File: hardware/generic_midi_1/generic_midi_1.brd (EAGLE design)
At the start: 47.3 x 44.8 mm, 20 parts, among them IC1 MEGA168/328, IC2 RFM12

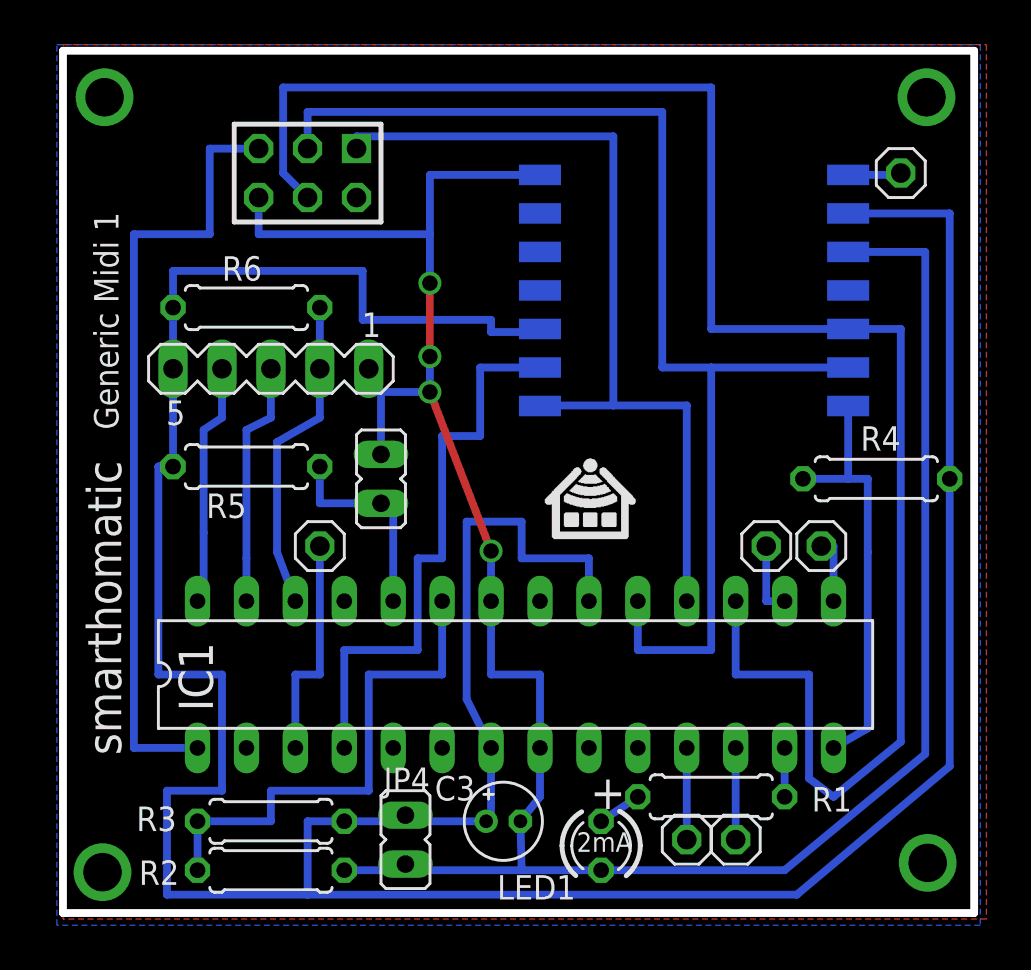
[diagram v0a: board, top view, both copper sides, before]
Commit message: add/rename some files, add I2C resistors to midi PCB
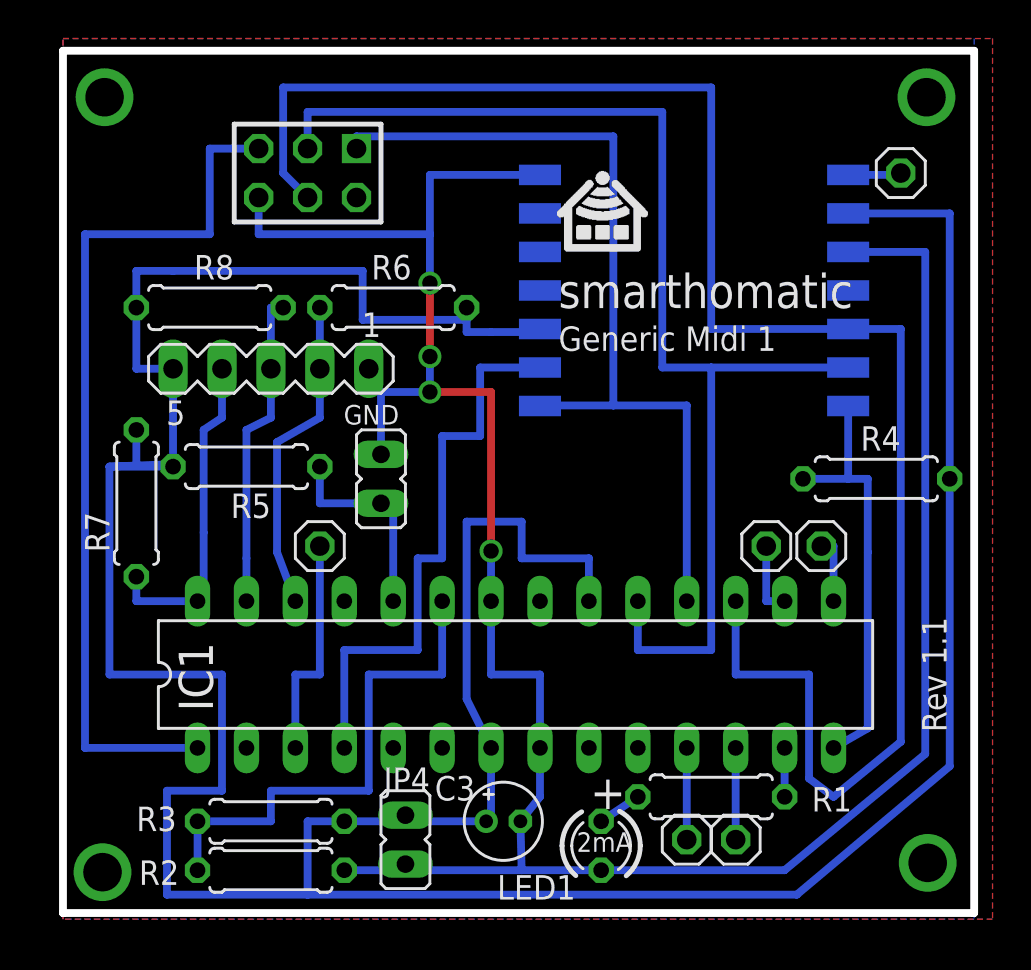
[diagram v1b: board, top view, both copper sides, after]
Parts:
- added R7, R8: 10k, rcl:0207/7
- JP2: value SHT15 -> I/O
- moved R6 7.62 mm to (17.1, 31.8), turned to 180 degrees
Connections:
- net N$7: now also R8.1
- net N$9: now also R7.1
- net VCC: now also R7.2, R8.2
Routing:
- net VCC: track 179.4 -> 193.9 mm
- net N$8: track 40.9 -> 46.0 mm
- net N$9: track 12.8 -> 17.3 mm
- net N$7: track 12.8 -> 16.7 mm
- net GND: track 126.1 -> 128.7 mm
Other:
- board text added: "GND"
- board text added: "Rev 1.1"
- board text removed: "Rev 1.0"

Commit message: update generic midi PCB
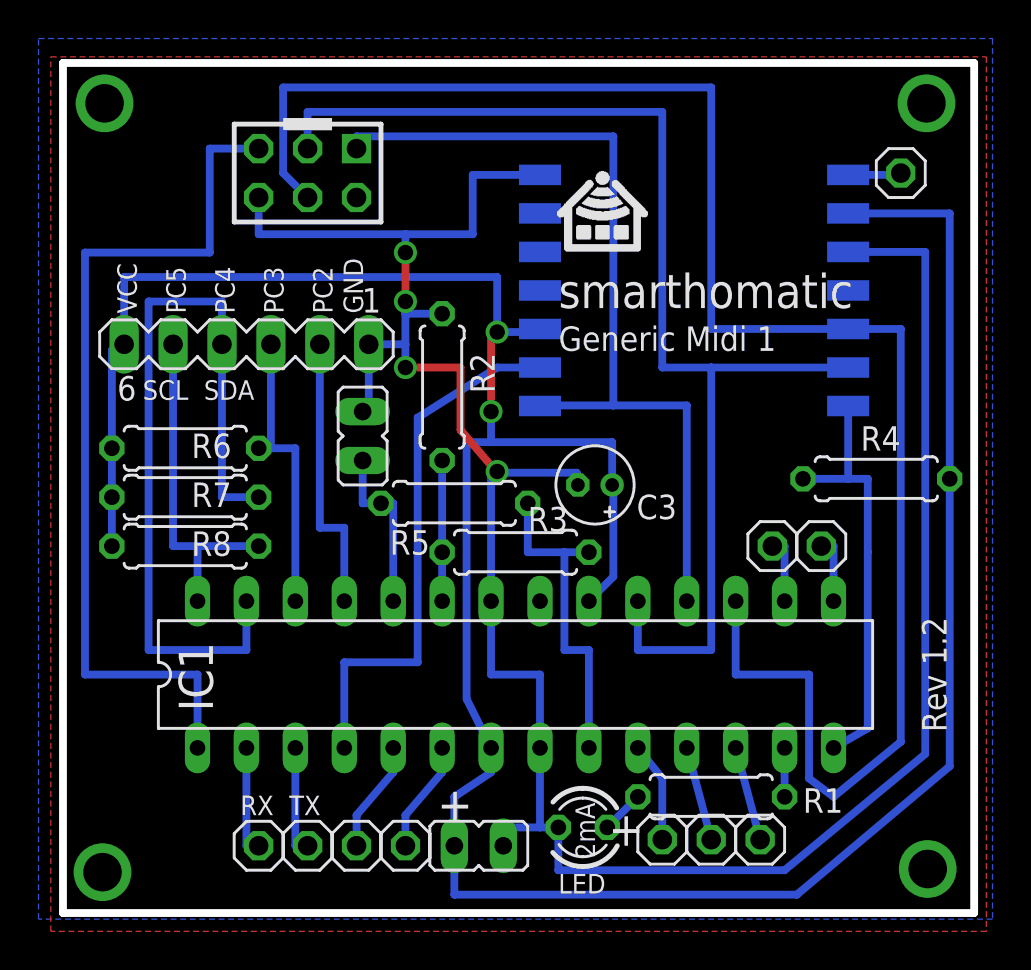
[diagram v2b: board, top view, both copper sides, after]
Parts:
- removed LED1: 2mA, led:LED3MM
- added JP11: PD4, pinhead:1X01
- added JP12: PD3, pinhead:1X01
- added JP13: PB7, pinhead:1X01
- added JP14: PD0, pinhead:1X01
- added LED: 2mA, led:LED3MM
- JP2: device con-lstb:MA05-1 -> con-lstb:MA06-1
- JP8: value PD1/TX -> PD1
- moved R2 26.6 mm to (19.7, 27.6), turned to 270 degrees
- moved R3 18.9 mm to (23.5, 19.1)
- moved C3 18.1 mm to (27.6, 22.5), turned to 180 degrees
- moved JP8 15.6 mm to (12.7, 3.81)
- moved R6 13.0 mm to (6.35, 24.4), turned to 0 degrees
- moved R8 12.4 mm to (6.35, 19.4)
- moved R5 11.0 mm to (20.3, 21.6), turned to 0 degrees
- moved JP4 3.82 mm to (21.6, 3.81), turned to 90 degrees
- moved R7 2.56 mm to (6.35, 21.9), turned to 180 degrees
- moved JP3 2.42 mm to (15.6, 25.1)
- moved JP2 1.80 mm to (9.53, 29.8)
- moved JP10 1.27 mm to (36.2, 4.13)
- moved JP9 1.27 mm to (33.7, 4.13)
- moved JP7 0.32 mm to (36.8, 19.4)
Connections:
- new net N$21: IC1.25, JP2.2
- new net N$22: IC1.6, JP11.1
- new net N$23: IC1.5, JP12.1
- new net N$24: IC1.9, R3.2, R5.2
- new net N$25: IC1.10, JP13.1
- new net N$26: IC1.2, JP14.1
- net GND: now also LED.K; no longer LED1.K
- net N$10: now also JP2.3; no longer JP2.2
- net N$12: now also LED.A; no longer LED1.A
- net N$7: now also JP2.4, R7.1; no longer JP2.3, R8.1
- net N$9: now also JP2.5, R8.1; no longer JP2.4, R7.1
- net VCC: now also JP2.6; no longer JP2.5, R3.2, R5.2
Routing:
- net VCC: track 193.9 -> 148.3 mm, vias 0 -> 2
- net N$7: track 16.7 -> 41.6 mm
- net N$18: track 26.7 -> 7.30 mm
- net N$24: track 0.00 -> 17.1 mm
- net N$21: track 0.00 -> 14.6 mm
- net N$20: track 11.7 -> 5.71 mm
- net N$23: track 0.00 -> 5.78 mm
- net N$22: track 0.00 -> 5.78 mm
- net N$26: track 0.00 -> 5.71 mm
- net N$25: track 0.00 -> 5.21 mm
- net N$1: track 10.8 -> 8.89 mm
- net N$15: track 29.9 -> 28.1 mm
- net GND: track 128.7 -> 127.0 mm
- net N$10: track 16.7 -> 15.9 mm
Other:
- board size 47.3 x 44.8 mm -> 47.3 x 44.1 mm
- board text added: "PC2"
- board text added: "PC3"
- board text added: "PC4"
- board text added: "PC5"
- board text added: "RX"
- board text added: "Rev 1.2"
- board text added: "SCL"
- board text added: "SDA"
- board text added: "TX"
- board text added: "VCC"
- board text removed: "Rev 1.1"

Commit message: Add pull-up resistor for possible one-wire sensor on PD4.
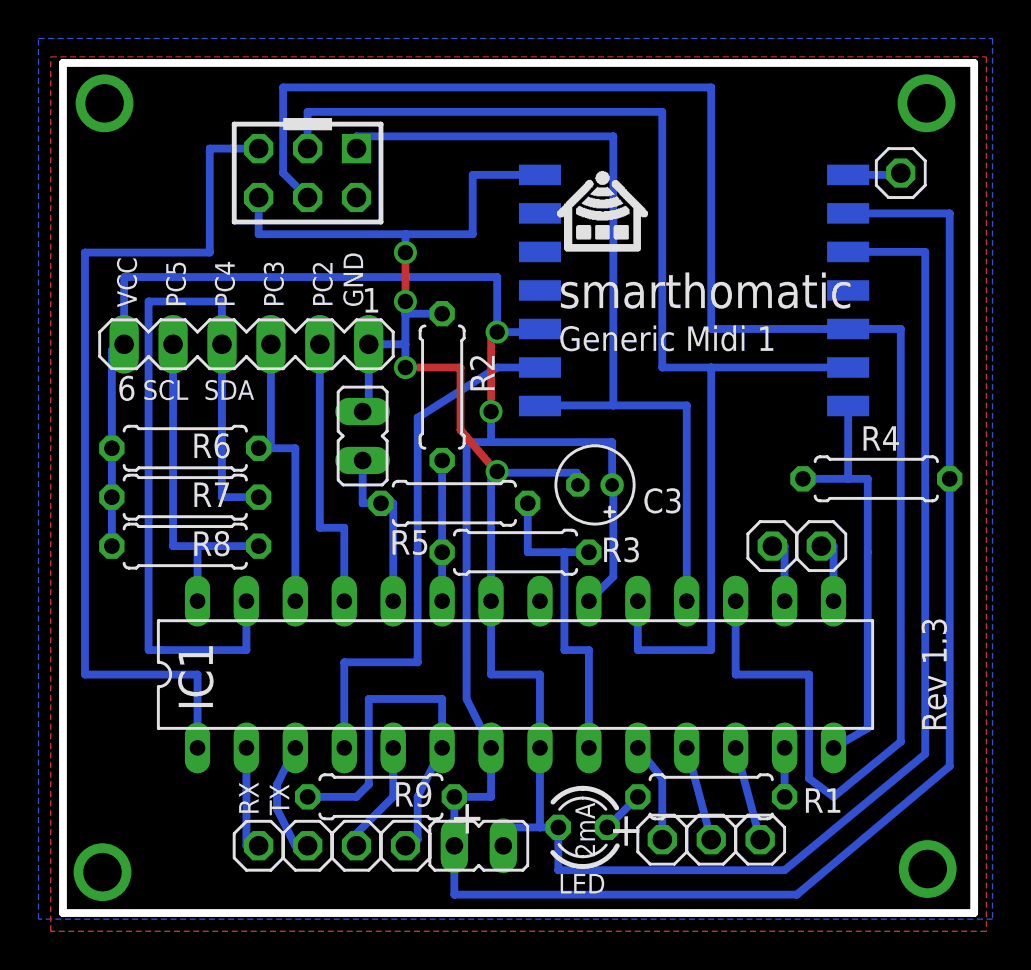
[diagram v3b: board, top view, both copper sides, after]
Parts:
- added R9: 4k7, rcl:0207/7
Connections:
- net N$22: now also R9.1
- net VCC: now also R9.2
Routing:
- net N$22: track 5.78 -> 20.0 mm
- net VCC: track 148.3 -> 149.2 mm
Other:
- board text added: "Rev 1.3"
- board text removed: "Rev 1.2"
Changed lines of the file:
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@@
 <wire x1="47.3075" y1="0.3175" x2="0" y2="0.3175" width="0.4064" layer="20"/>
 <text x="25.7302" y="31.7246" size="1.778" layer="25" font="vector">smarthomatic</text>
-<text x="44.6024" y="15.6845" size="1.27" layer="25" rot="R270">Rev 1.2</text>
+<text x="44.6024" y="15.6845" size="1.27" layer="25" rot="R270">Rev 1.3</text>
 <rectangle x1="26.109928125" y1="34.65195" x2="29.907228125" y2="34.68496875" layer="25"/>
 <rectangle x1="26.076909375" y1="34.68496875" x2="29.973265625" y2="34.7179875" layer="25"/>
@@
 <text x="30.1625" y="3.81" size="1.778" layer="25" rot="MR0">+</text>
 <text x="27.6225" y="3.175" size="1.016" layer="25" rot="R90">2mA</text>
-<text x="15.5829" y="31.4452" size="1.016" layer="25" rot="R90">GND</text>
-<text x="21.2725" y="5.08" size="1.778" layer="25" rot="MR0">+</text>
+<text x="15.5829" y="31.7627" size="1.016" layer="25" rot="R90">GND</text>
+<text x="21.9075" y="4.445" size="1.778" layer="25" rot="MR0">+</text>
 <rectangle x1="11.43" y1="40.9575" x2="13.97" y2="41.5925" layer="21"/>
-<text x="9.2075" y="5.3975" size="1.016" layer="25">RX</text>
-<text x="11.7475" y="5.3975" size="1.016" layer="25">TX</text>
-<text x="3.8354" y="31.4452" size="1.016" layer="25" rot="R90">VCC</text>
-<text x="13.9954" y="31.4452" size="1.016" layer="25" rot="R90">PC2</text>
-<text x="11.4554" y="31.4452" size="1.016" layer="25" rot="R90">PC3</text>
-<text x="8.9154" y="31.4452" size="1.016" layer="25" rot="R90">PC4</text>
-<text x="6.3754" y="31.4452" size="1.016" layer="25" rot="R90">PC5</text>
+<text x="10.16" y="5.3975" size="1.016" layer="25" rot="R90">RX</text>
+<text x="11.7475" y="5.3975" size="1.016" layer="25" rot="R90">TX</text>
+<text x="3.8354" y="31.7627" size="1.016" layer="25" rot="R90">VCC</text>
+<text x="13.9954" y="31.7627" size="1.016" layer="25" rot="R90">PC2</text>
+<text x="11.4554" y="31.7627" size="1.016" layer="25" rot="R90">PC3</text>
+<text x="8.9154" y="31.7627" size="1.016" layer="25" rot="R90">PC4</text>
+<text x="6.3754" y="31.7627" size="1.016" layer="25" rot="R90">PC5</text>
 <text x="7.3152" y="26.9621" size="1.016" layer="25">SDA</text>
 <text x="4.1402" y="26.9621" size="1.016" layer="25">SCL</text>
@@
 </element>
 <element name="C3" library="rcl" package="E1,8-4" value="10µ" x="27.6225" y="22.5425" smashed="yes" rot="R180">
-<attribute name="NAME" x="29.7815" y="20.7645" size="1.27" layer="25" ratio="10"/>
-<attribute name="VALUE" x="29.7815" y="22.352" size="1.27" layer="27" ratio="10"/>
+<attribute name="NAME" x="30.099" y="21.082" size="1.27" layer="25" ratio="10"/>
+<attribute name="VALUE" x="30.099" y="22.6695" size="1.27" layer="27" ratio="10"/>
 </element>
 <element name="R2" library="rcl" package="0207/7" value="150k" x="19.685" y="27.6225" smashed="yes" rot="R270">
@@
 </element>
 <element name="R3" library="rcl" package="0207/7" value="330k" x="23.495" y="19.05" smashed="yes">
-<attribute name="NAME" x="24.13" y="20.1295" size="1.27" layer="25" ratio="10"/>
+<attribute name="NAME" x="27.94" y="18.542" size="1.27" layer="25" ratio="10"/>
 <attribute name="VALUE" x="25.4635" y="19.6088" size="1.27" layer="27" ratio="10" rot="R180"/>
 </element>
@@
 </element>
 <element name="JP3" library="jumper" package="JP1" value="PHOTO" x="15.5575" y="25.0825" smashed="yes" rot="R180">
-<attribute name="VALUE" x="14.0335" y="23.1775" size="0.8128" layer="27" ratio="10" rot="R90"/>
+<attribute name="VALUE" x="13.716" y="23.1775" size="0.8128" layer="27" ratio="10" rot="R90"/>
 </element>
 <element name="JP4" library="jumper" package="JP1" value="PWR" x="21.59" y="3.81" smashed="yes" rot="R90">
@@
 <element name="JP14" library="pinhead" package="1X01" value="PD0" x="10.16" y="3.81" smashed="yes">
 <attribute name="VALUE" x="7.9375" y="1.27" size="1.016" layer="27"/>
+</element>
+<element name="R9" library="rcl" package="0207/7" value="4k7" x="16.51" y="6.35" smashed="yes">
+<attribute name="NAME" x="17.145" y="5.842" size="1.27" layer="25" ratio="10"/>
+<attribute name="VALUE" x="13.589" y="5.7912" size="1.27" layer="27" ratio="10"/>
 </element>
 </elements>
@@
 <wire x1="2.54" y1="21.9075" x2="2.54" y2="19.3675" width="0.4064" layer="16"/>
 <wire x1="20.32" y1="3.81" x2="20.32" y2="1.27" width="0.4064" layer="16"/>
-<wire x1="20.32" y1="3.81" x2="20.32" y2="6.35" width="0.4064" layer="16"/>
-<wire x1="20.32" y1="6.35" x2="22.225" y2="7.62" width="0.4064" layer="16"/>
 <wire x1="22.225" y1="7.62" x2="22.225" y2="8.89" width="0.4064" layer="16"/>
+<contactref element="R9" pad="2"/>
+<wire x1="20.32" y1="6.35" x2="22.225" y2="6.35" width="0.4064" layer="16"/>
+<wire x1="22.225" y1="6.35" x2="22.225" y2="7.62" width="0.4064" layer="16"/>
 <wire x1="28.5115" y1="22.5425" x2="28.575" y2="22.5425" width="0" layer="19" extent="16-16"/>
+<wire x1="20.32" y1="6.35" x2="20.32" y2="3.81" width="0.4064" layer="16"/>
 </signal>
 <signal name="N$3">
@@
 <contactref element="JP8" pad="1"/>
 <wire x1="12.7" y1="3.81" x2="12.065" y2="3.81" width="0.4064" layer="16"/>
-<wire x1="12.065" y1="3.81" x2="12.065" y2="8.89" width="0.4064" layer="16"/>
+<wire x1="12.065" y1="3.81" x2="11.1125" y2="5.715" width="0.4064" layer="16"/>
+<wire x1="11.1125" y1="5.715" x2="11.1125" y2="6.985" width="0.4064" layer="16"/>
+<wire x1="11.1125" y1="6.985" x2="12.065" y2="8.89" width="0.4064" layer="16"/>
 </signal>
 <signal name="N$21">
@@
 <contactref element="IC1" pad="6"/>
 <contactref element="JP11" pad="1"/>
-<wire x1="17.78" y1="3.81" x2="17.78" y2="5.3975" width="0.4064" layer="16"/>
-<wire x1="17.78" y1="5.3975" x2="19.685" y2="7.62" width="0.4064" layer="16"/>
-<wire x1="19.685" y1="7.62" x2="19.685" y2="8.89" width="0.4064" layer="16"/>
+<wire x1="17.78" y1="3.81" x2="18.415" y2="4.1275" width="0.4064" layer="16"/>
+<wire x1="18.415" y1="4.1275" x2="18.415" y2="6.35" width="0.4064" layer="16"/>
+<wire x1="18.415" y1="6.35" x2="19.685" y2="8.89" width="0.4064" layer="16"/>
+<contactref element="R9" pad="1"/>
+<wire x1="12.7" y1="6.35" x2="15.24" y2="6.35" width="0.4064" layer="16"/>
+<wire x1="15.24" y1="6.35" x2="15.875" y2="6.985" width="0.4064" layer="16"/>
+<wire x1="15.875" y1="6.985" x2="15.875" y2="11.43" width="0.4064" layer="16"/>
+<wire x1="15.875" y1="11.43" x2="19.685" y2="11.43" width="0.4064" layer="16"/>
+<wire x1="19.685" y1="11.43" x2="19.685" y2="8.89" width="0.4064" layer="16"/>
 </signal>
 <signal name="N$23">
 <contactref element="IC1" pad="5"/>
 <contactref element="JP12" pad="1"/>
-<wire x1="15.24" y1="3.81" x2="15.24" y2="5.3975" width="0.4064" layer="16"/>
-<wire x1="15.24" y1="5.3975" x2="17.145" y2="7.62" width="0.4064" layer="16"/>
-<wire x1="17.145" y1="7.62" x2="17.145" y2="8.89" width="0.4064" layer="16"/>
+<wire x1="15.24" y1="3.81" x2="15.24" y2="4.445" width="0.4064" layer="16"/>
+<wire x1="15.24" y1="4.445" x2="17.145" y2="6.35" width="0.4064" layer="16"/>
+<wire x1="17.145" y1="6.35" x2="17.145" y2="8.89" width="0.4064" layer="16"/>
 </signal>
 <signal name="N$24">

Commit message: Add solder jumper to PCB for ISP VCC pin.
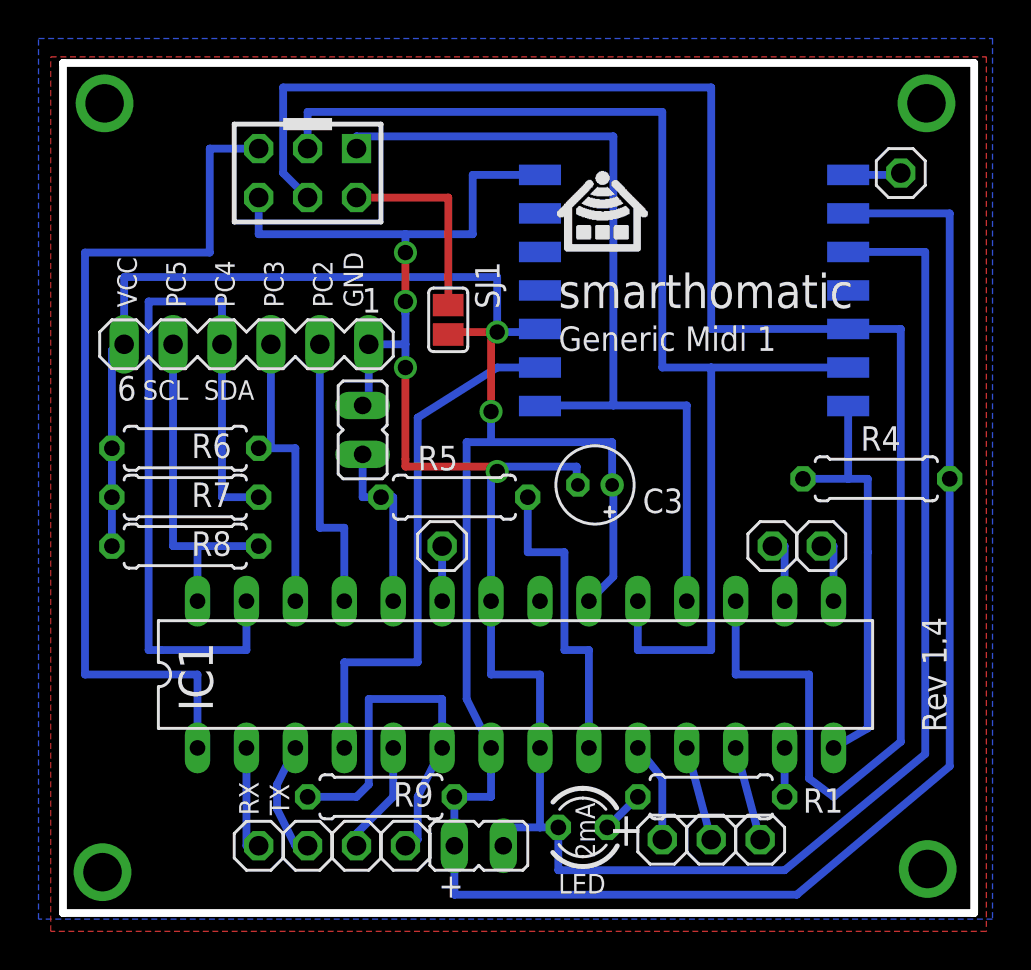
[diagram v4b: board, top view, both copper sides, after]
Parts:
- removed R2: 150k, rcl:0207/7
- removed R3: 330k, rcl:0207/7
- added JP15: PC0, pinhead:1X01
- added SJ1: VCC, jumper:SJ
- moved JP3 0.32 mm to (15.6, 25.4)
- moved R5 0.32 mm to (20.3, 21.9)
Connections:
- new net N$27: JP1.2, SJ1.1
- net GND: no longer R2.1
- net N$18: now also JP15.1; no longer R2.2, R3.1
- net N$24: no longer R3.2
- net VCC: now also SJ1.2
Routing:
- net N$27: track 0.00 -> 10.4 mm
- net N$18: track 7.30 -> 2.86 mm
- net VCC: track 149.2 -> 151.9 mm
- net N$24: track 17.1 -> 16.2 mm
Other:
- board text added: "Rev 1.4"
- board text removed: "Rev 1.3"
